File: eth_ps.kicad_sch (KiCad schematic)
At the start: 41 parts, among them J24 RJ45_RB1-125B8G1A, U32 RTL8211F-CG, Y4 SX5B25.000F1220F30

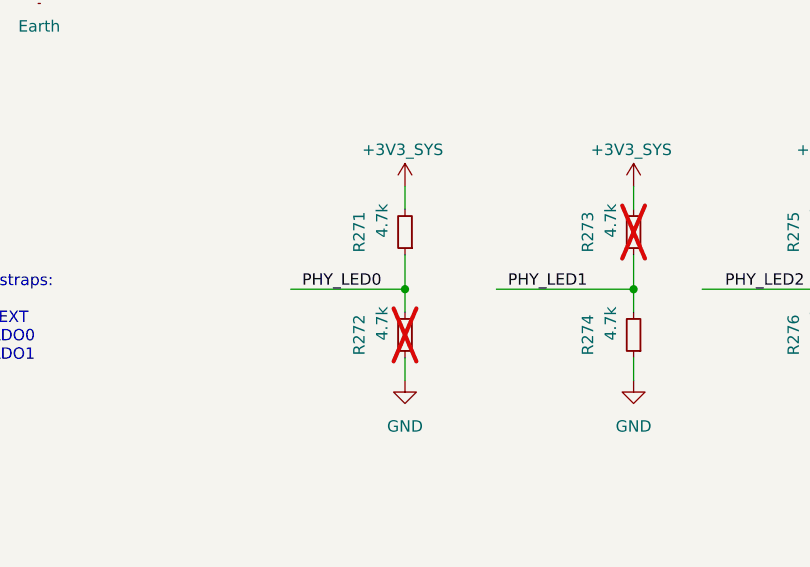
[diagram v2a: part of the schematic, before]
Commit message: schema: PHY_LED0 is tied to gnd to enable the internal 1V0 in PS ETH PHY.
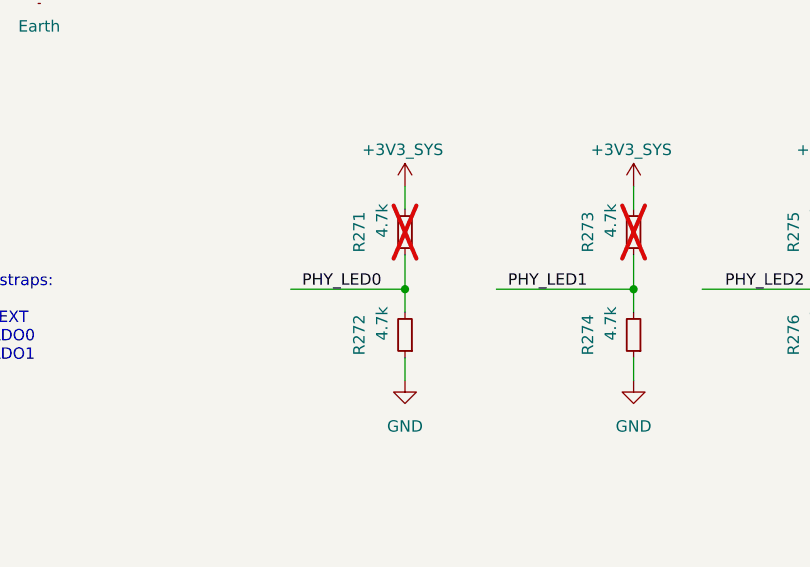
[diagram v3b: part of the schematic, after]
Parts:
- R271: now not fitted
- R272: now fitted
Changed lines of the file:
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@@
 		(in_bom yes)
 		(on_board yes)
-		(dnp no)
+		(dnp yes)
 		(property "Reference" "R271"
 			(at 342.9 165.1 90)
@@
 		(in_bom yes)
 		(on_board yes)
-		(dnp yes)
+		(dnp no)
 		(property "Reference" "R272"
 			(at 342.9 176.53 90)
